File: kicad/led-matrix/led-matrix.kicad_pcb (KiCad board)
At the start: 2 copper layers, 14 parts, among them J1 INPUT_CONN, J2 OUTPUT_CONN, U1 74HCT4051, U2 MIC2981_82YN, U3 TPIC6C595N

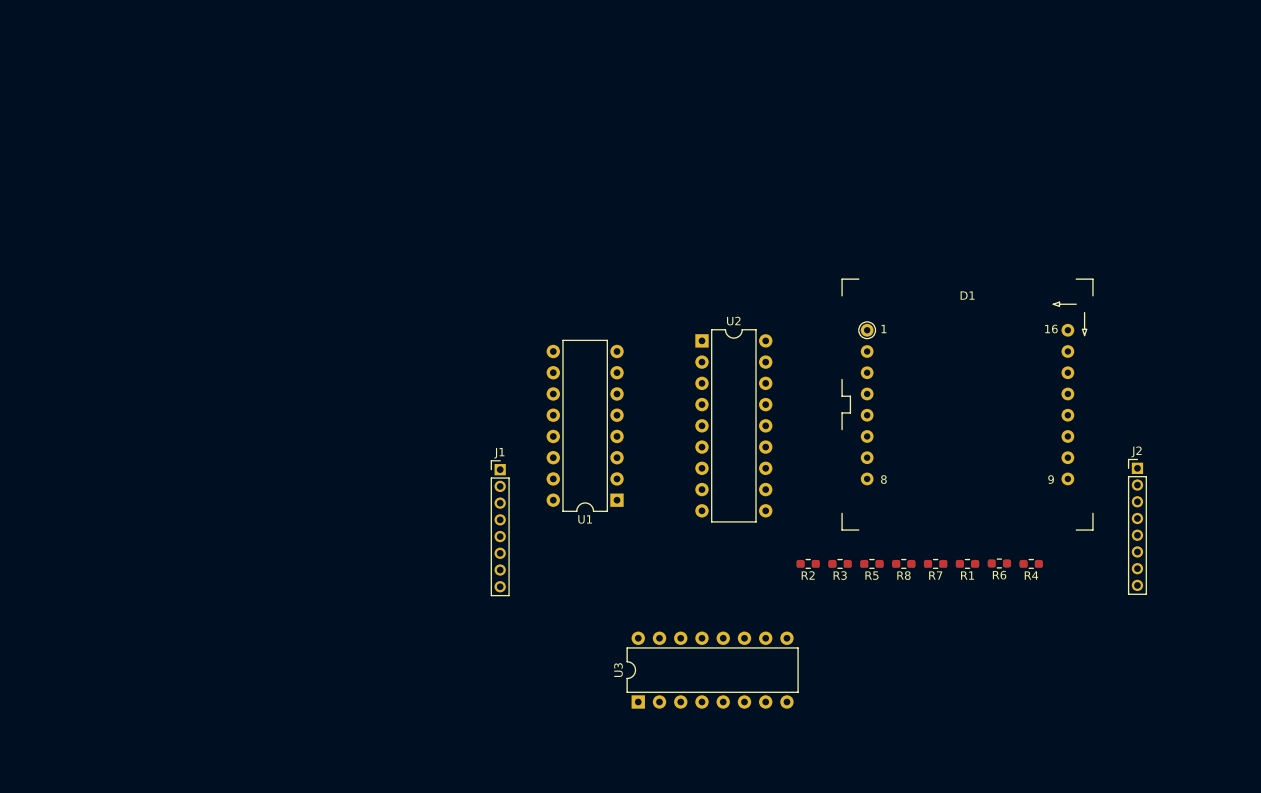
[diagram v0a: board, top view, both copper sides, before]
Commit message: Kicad: PCB: Add GND planes
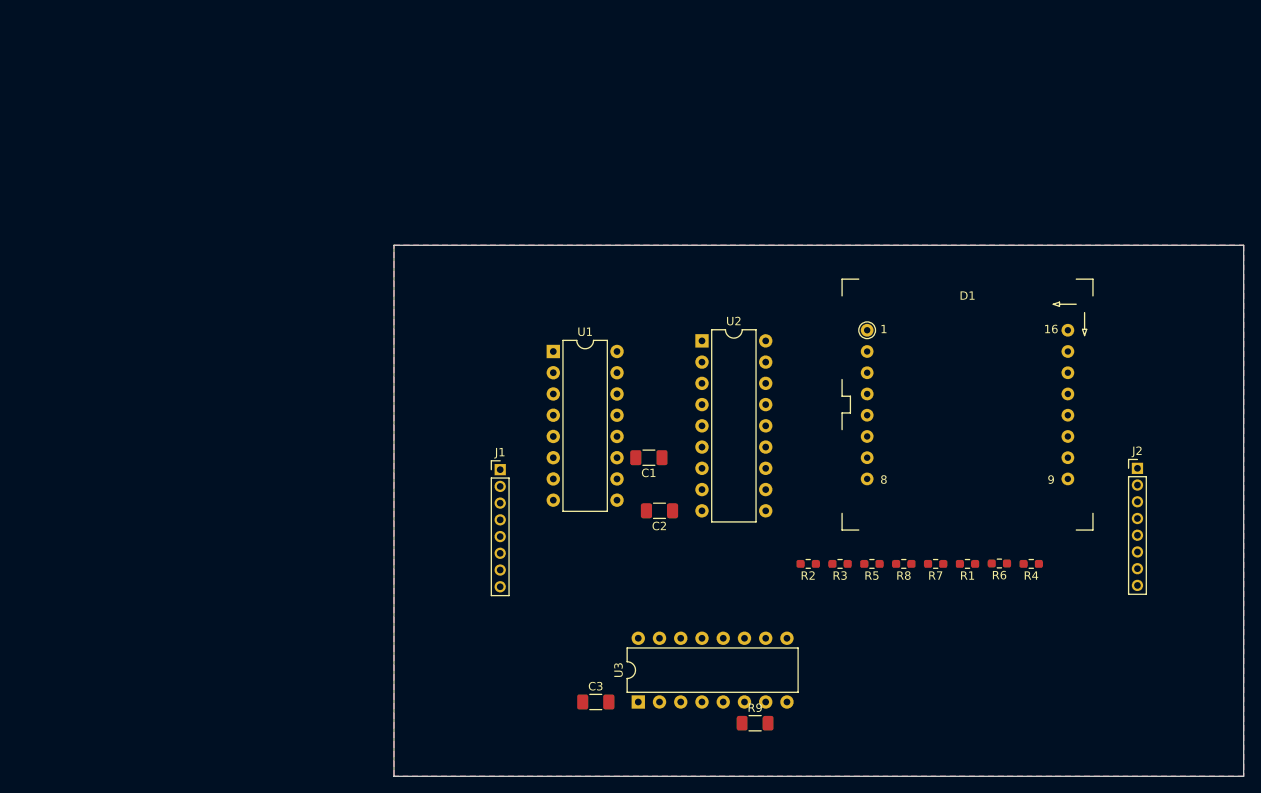
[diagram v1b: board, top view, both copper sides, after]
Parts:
- added C1: 100 nF, Capacitor_SMD:C_1206_3216Metric_Pad1.33x1.80mm_HandSolder, F.Cu at (94.0, 76.2)
- added C2: 100 nF, Capacitor_SMD:C_1206_3216Metric_Pad1.33x1.80mm_HandSolder, F.Cu at (95.2, 82.5)
- added C3: 100 nF, Capacitor_SMD:C_1206_3216Metric_Pad1.33x1.80mm_HandSolder, F.Cu at (87.6, 105.4)
- added R9: 10k, Resistor_SMD:R_1206_3216Metric_Pad1.30x1.75mm_HandSolder, F.Cu at (106.7, 108.0)
- moved U1 19.3 mm to (82.5, 63.5), turned to 0 degrees
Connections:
- U3 pad 7: /VCC -> Net-(R9-Pad2)
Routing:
- added copper zone on B.Cu, net /GND
- added copper zone on F.Cu, net /GND
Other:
- board outline added: 101.6 x 63.5 mm

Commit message: Organized components and placed headers
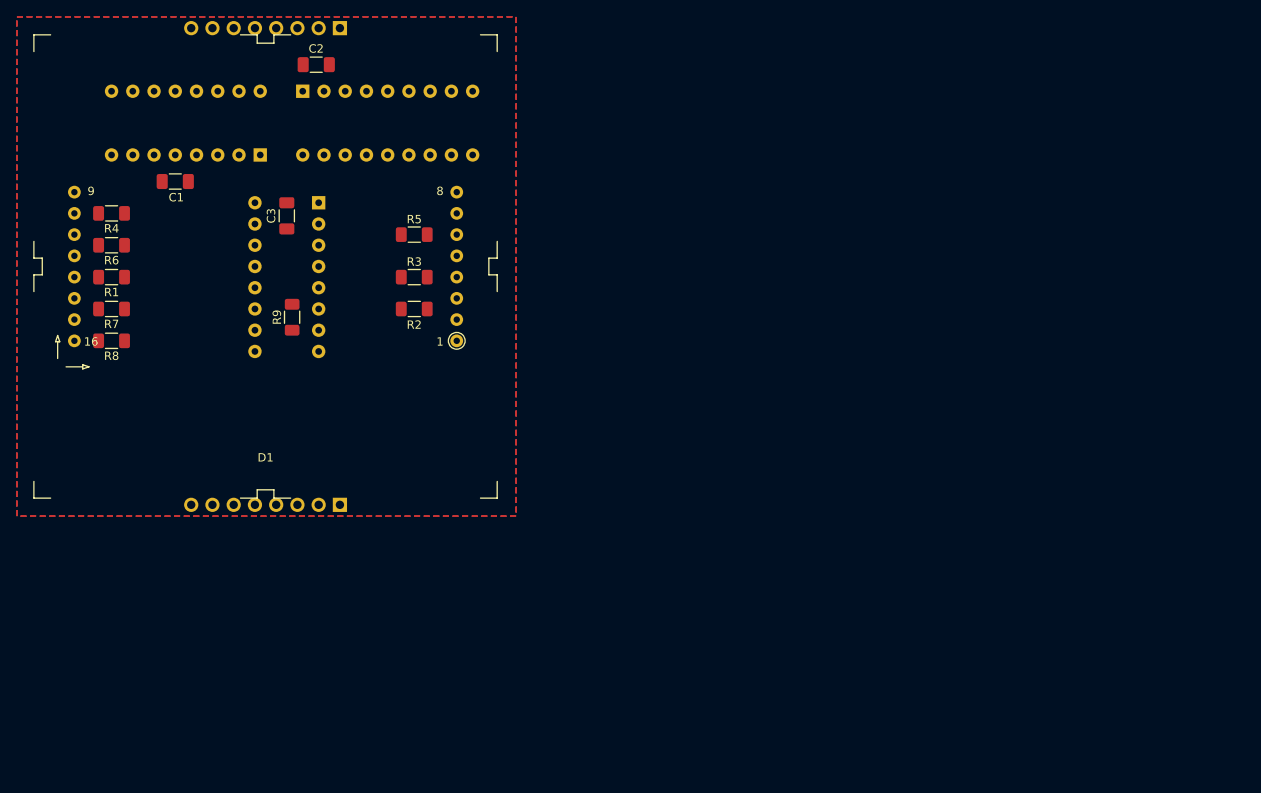
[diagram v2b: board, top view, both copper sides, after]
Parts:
- D1: footprint akn_misc:LED_8x8_3MM_32x32MM -> akn_misc:LED_8x8_7.62MM_60.2x60.2MM
- J1: footprint Connector_PinHeader_2.00mm:PinHeader_1x08_P2.00mm_Vertical -> Connector_PinSocket_2.54mm:PinSocket_1x08_P2.54mm_Horizontal; moved to B.Cu
- J2: footprint Connector_PinHeader_2.00mm:PinHeader_1x08_P2.00mm_Vertical -> Connector_PinHeader_2.54mm:PinHeader_1x08_P2.54mm_Horizontal; moved to B.Cu
- R1, R2, R3, R4, R5, R6, R7, R8: footprint Resistor_SMD:R_0603_1608Metric_Pad0.98x0.95mm_HandSolder -> Resistor_SMD:R_1206_3216Metric_Pad1.30x1.75mm_HandSolder
- U1, U2, U3: moved to B.Cu
- moved R4 117.7 mm to (29.7, 47.0)
- moved R6 112.8 mm to (29.7, 50.8)
- moved J2 108.9 mm to (57.0, 24.8), turned to 90 degrees
- moved R1 107.9 mm to (29.7, 54.6)
- moved R7 103.1 mm to (29.7, 58.4)
- moved R8 98.4 mm to (29.7, 62.2)
- moved D1 85.5 mm to (48.1, 53.3), turned to 180 degrees
- moved R9 73.6 mm to (51.3, 59.4), turned to 270 degrees
- moved U3 70.9 mm to (54.5, 45.7), turned to 180 degrees
- moved C3 68.9 mm to (50.7, 47.3), turned to 90 degrees
- moved R5 67.4 mm to (65.9, 49.5), turned to 0 degrees
- moved C2 67.3 mm to (54.2, 29.2)
- moved C1 65.6 mm to (37.4, 43.2), turned to 0 degrees
- moved R3 61.4 mm to (65.9, 54.6), turned to 0 degrees
- moved U2 56.3 mm to (52.6, 32.4), turned to 270 degrees
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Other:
- board outline removed

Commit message: Routing left side and upper ICs
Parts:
- moved R9 5.39 mm to (50.8, 64.8), turned to 90 degrees
- moved C3 2.55 mm to (52.7, 45.7), turned to 0 degrees
- moved U3 2.54 mm to (54.5, 48.3)
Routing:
- net /VCC: track 0.00 -> 42.1 mm
- net /a4: track 0.00 -> 37.9 mm
- net /b4: track 0.00 -> 37.1 mm
- net /a5: track 0.00 -> 32.8 mm
- net /b6: track 0.00 -> 26.9 mm
- net /a6: track 0.00 -> 26.0 mm
- net /a3: track 0.00 -> 25.1 mm
- net /b2: track 0.00 -> 16.9 mm
- net /a1: track 0.00 -> 15.4 mm
- net /a2: track 0.00 -> 14.5 mm
- net /b7: track 0.00 -> 14.0 mm
- net /a0: track 0.00 -> 13.7 mm
- net /b5: track 0.00 -> 9.35 mm

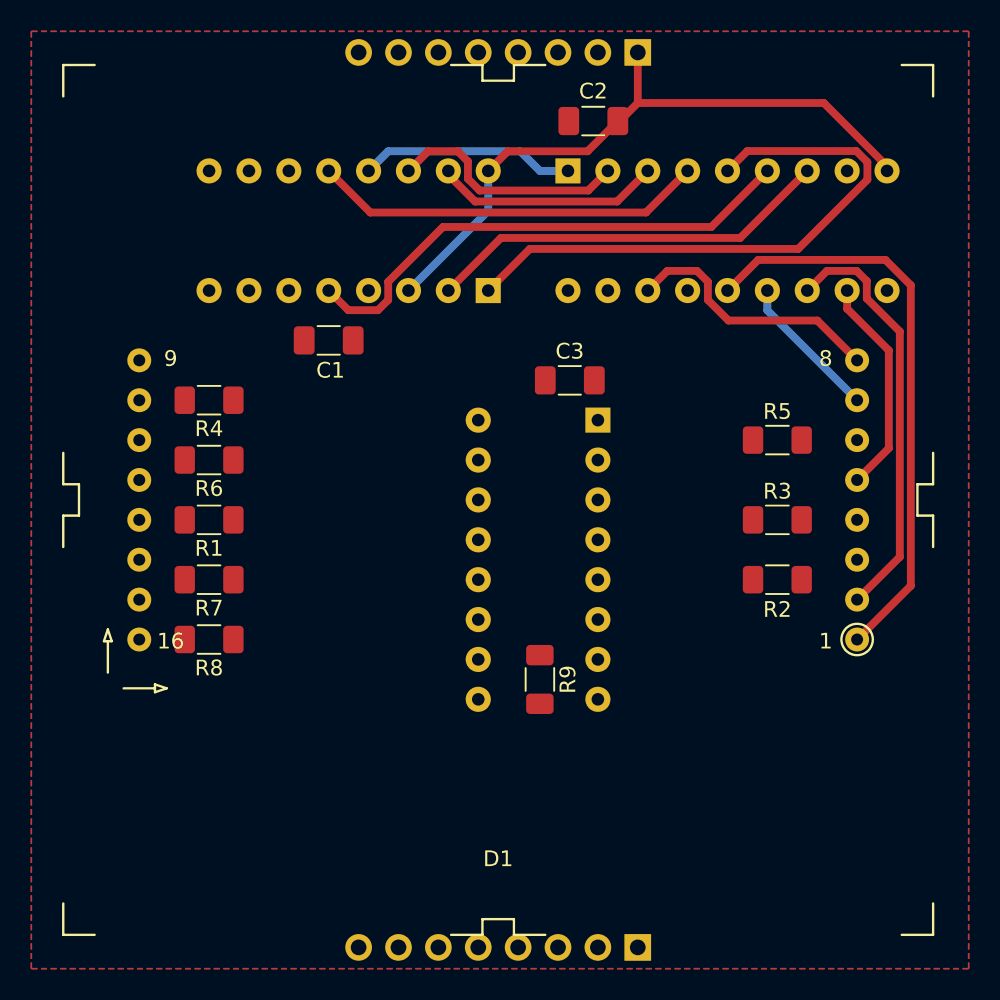
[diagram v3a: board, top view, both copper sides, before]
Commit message: Complete routing and clear up ground planes
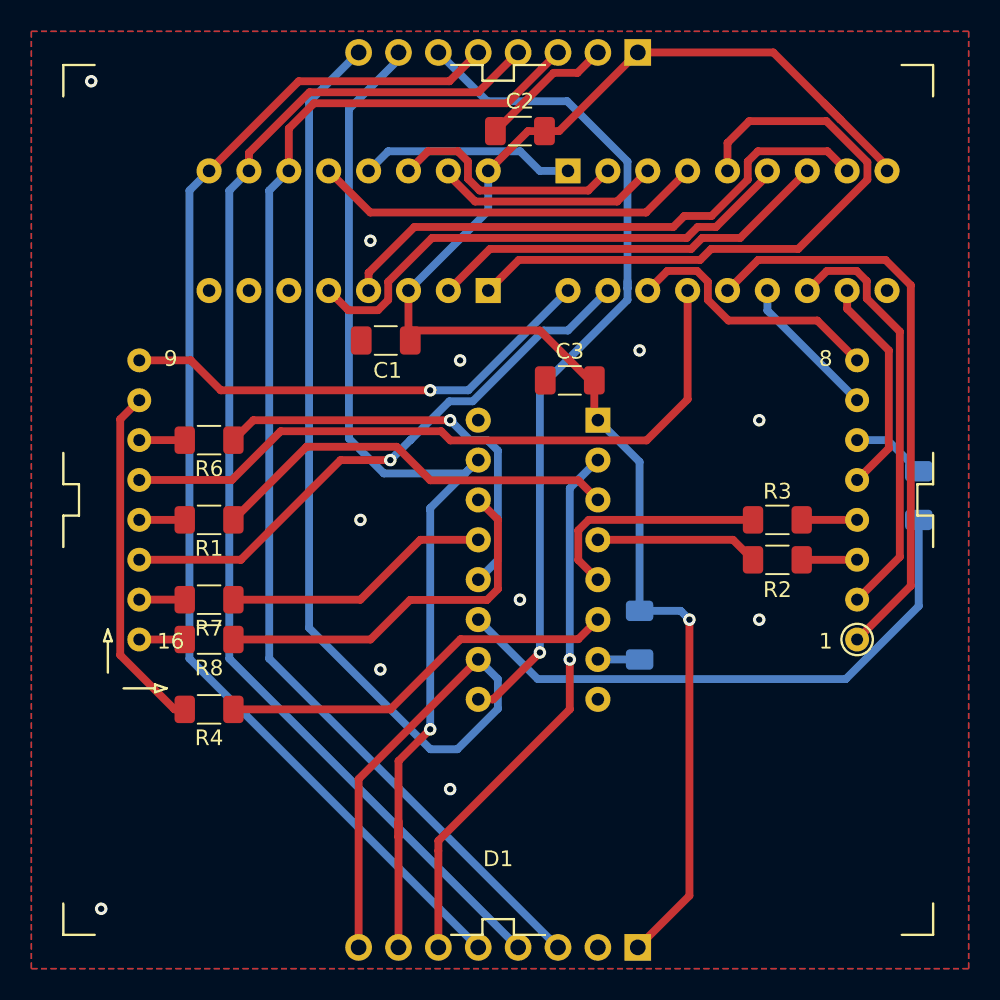
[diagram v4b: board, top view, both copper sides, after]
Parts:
- R5, R9: moved to B.Cu
- moved R4 19.7 mm to (29.7, 66.7)
- moved R5 9.67 mm to (74.9, 53.1), turned to 90 degrees
- moved R9 6.95 mm to (57.1, 62.0), turned to 270 degrees
- moved C2 4.72 mm to (49.5, 29.8)
- moved C1 3.63 mm to (41.0, 43.2)
- moved R7 1.27 mm to (29.7, 59.7)
- moved R2 1.27 mm to (65.9, 57.1)
- moved R6 1.27 mm to (29.7, 49.5)
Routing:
- net /s0: track 0.00 -> 79.4 mm
- net /r_clk: track 0.00 -> 79.4 mm
- net /s1: track 0.00 -> 79.1 mm
- net /s2: track 0.00 -> 77.9 mm
- net /serial_clk: track 0.00 -> 69.6 mm, vias 0 -> 1
- net /VCC: track 42.1 -> 100.5 mm, vias 0 -> 1
- net /serial_out: track 0.00 -> 54.1 mm, vias 0 -> 1
- net /b3: track 0.00 -> 44.5 mm
- net /d4: track 0.00 -> 37.0 mm
- net /b1: track 0.00 -> 37.0 mm, vias 0 -> 1
- net /a7: track 0.00 -> 36.0 mm
- net /serial_in: track 0.00 -> 35.2 mm, vias 0 -> 1
- net /b0: track 0.00 -> 30.7 mm, vias 0 -> 1
- net /d5: track 0.00 -> 26.9 mm, vias 0 -> 1
- net /d0: track 0.00 -> 26.6 mm
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
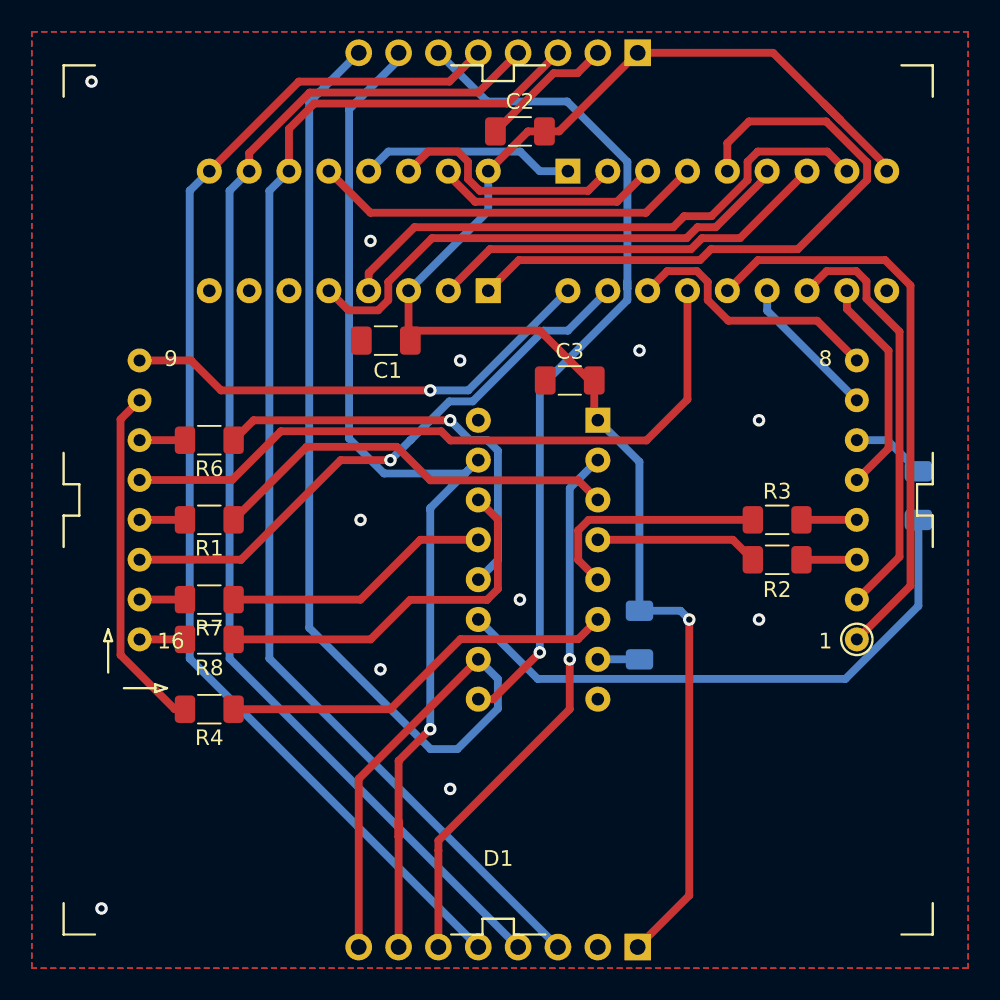
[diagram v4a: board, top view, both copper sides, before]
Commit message: Updated 3D model and fixed Edge.Cuts layer
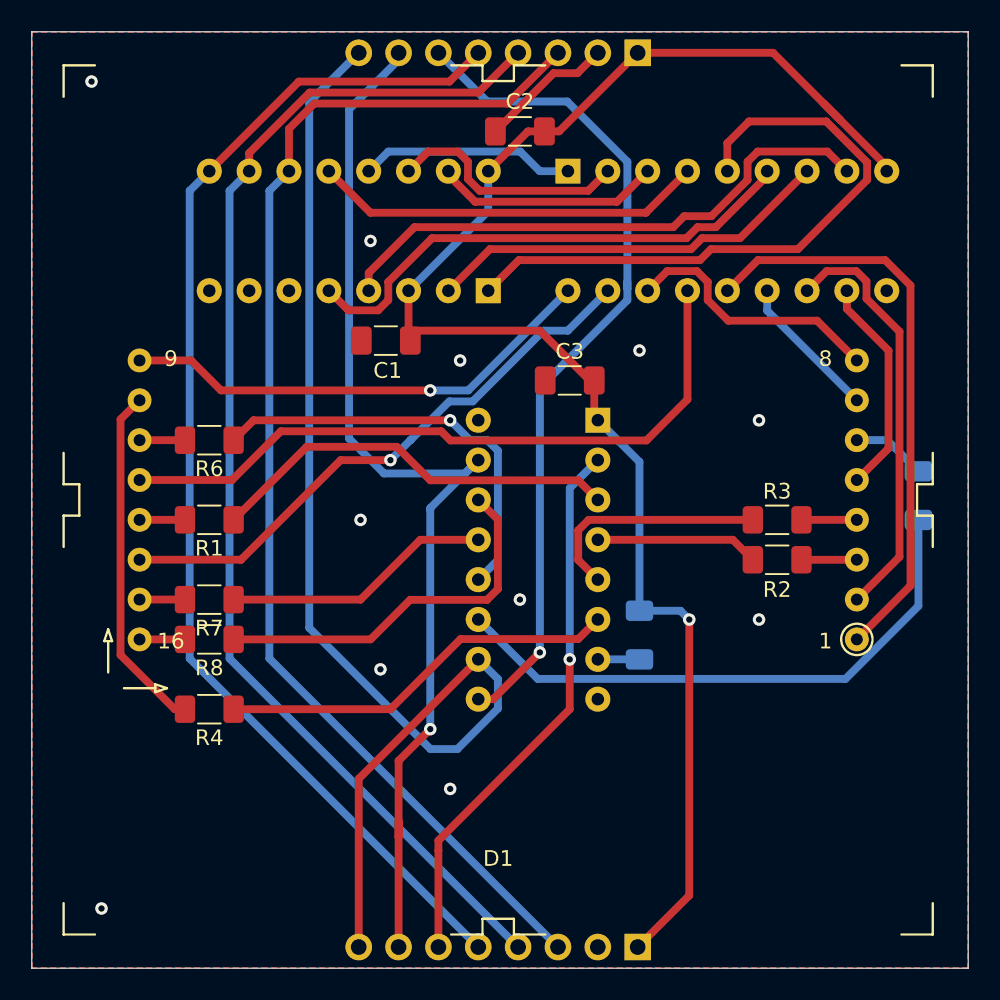
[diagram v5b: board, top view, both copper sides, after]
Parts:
- D1: footprint akn_misc:LED_8x8_7.62MM_60.2x60.2MM -> led_matrix:LED_8x8_7.62MM_60.2x60.2MM
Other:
- board outline added: 59.7 x 59.7 mm
